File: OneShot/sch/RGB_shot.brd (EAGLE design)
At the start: 20 x 20 mm, 20 parts, among them Q1 BC846ALT1SMD, Q2 BC846ALT1SMD, Q3 BC846ALT1SMD

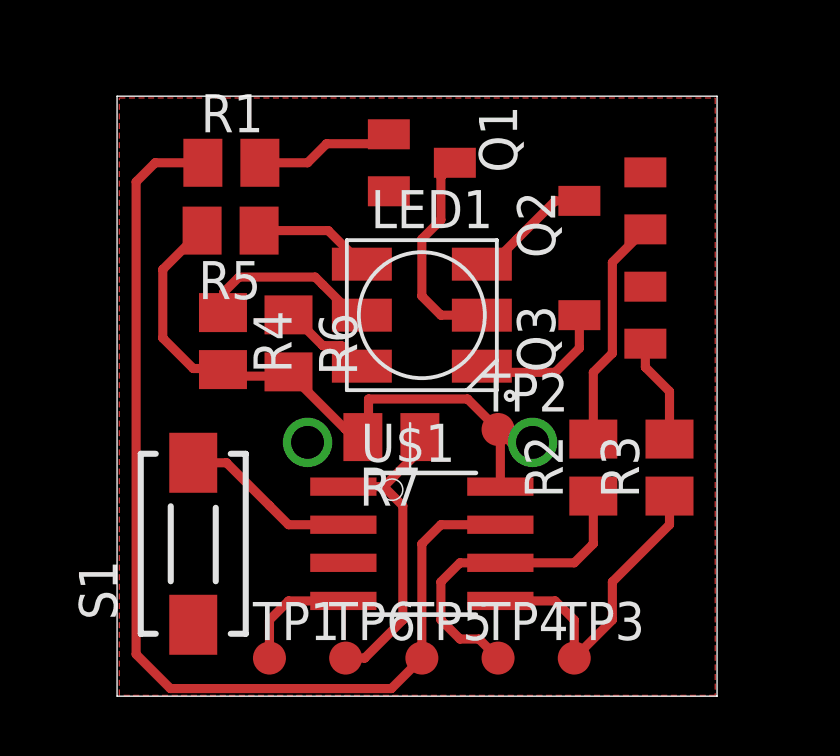
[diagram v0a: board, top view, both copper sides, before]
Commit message: Fix wire spacing
More spacing between wire for freely laser-iron production
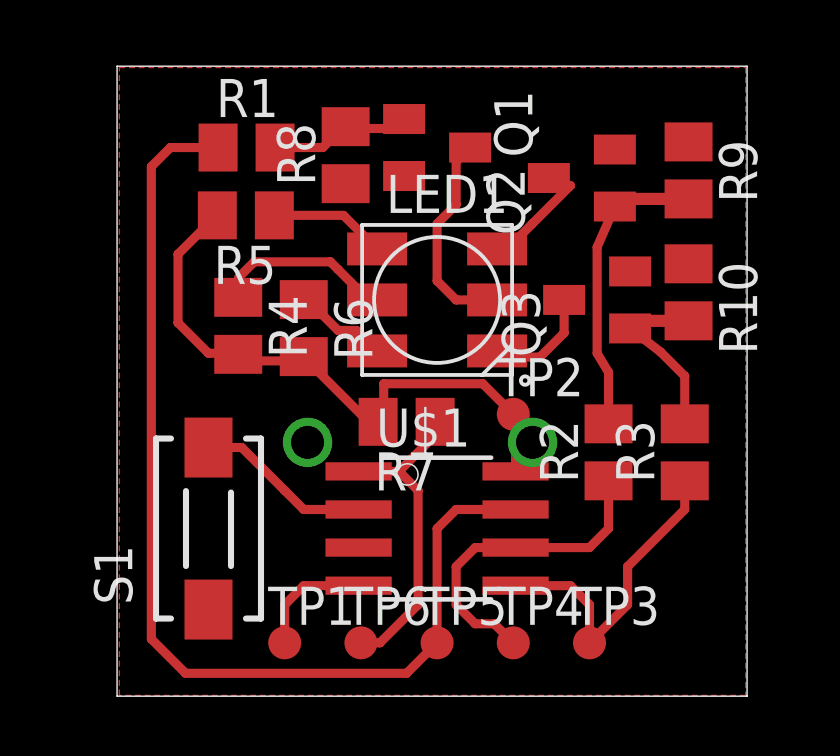
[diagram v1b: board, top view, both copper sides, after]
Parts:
- added R10, R8, R9: (no value), resistor:M0805
- moved Q2 1.27 mm to (15.5, 17.3)
- moved Q3 0.72 mm to (16.0, 13.2)
- moved R5 0.72 mm to (4.29, 16.0)
- moved R6 0.72 mm to (6.22, 12.3)
- moved TP4 0.72 mm to (13.2, 1.78)
- moved R4 0.72 mm to (4.04, 12.3)
- moved LED1 0.72 mm to (10.7, 13.2)
- moved R7 0.72 mm to (9.65, 9.14)
- moved TP2 0.72 mm to (13.2, 9.40)
- moved S1 0.72 mm to (3.05, 5.59)
- moved TP1 0.72 mm to (5.59, 1.78)
- moved TP6 0.72 mm to (8.13, 1.78)
- moved R2 0.72 mm to (16.4, 8.13)
- moved R3 0.72 mm to (18.9, 8.13)
- moved TP3 0.72 mm to (15.7, 1.78)
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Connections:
- net GND: now also R10.1, R8.1, R9.1
- net N$10: now also R9.2
- net N$11: now also R10.2
- net N$9: now also R8.2
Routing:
- net N$10: track 7.71 -> 10.3 mm
- net N$11: track 3.83 -> 6.43 mm
- net N$8: track 4.77 -> 3.75 mm
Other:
- board size 20 x 20 mm -> 21 x 21 mm
